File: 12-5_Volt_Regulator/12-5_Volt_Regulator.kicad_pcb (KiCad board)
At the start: 2 copper layers, 44.4 x 31.8 mm, 23 parts, among them J1 Conn_01x02, J2 Conn_01x02, U1 LM22676MR-5

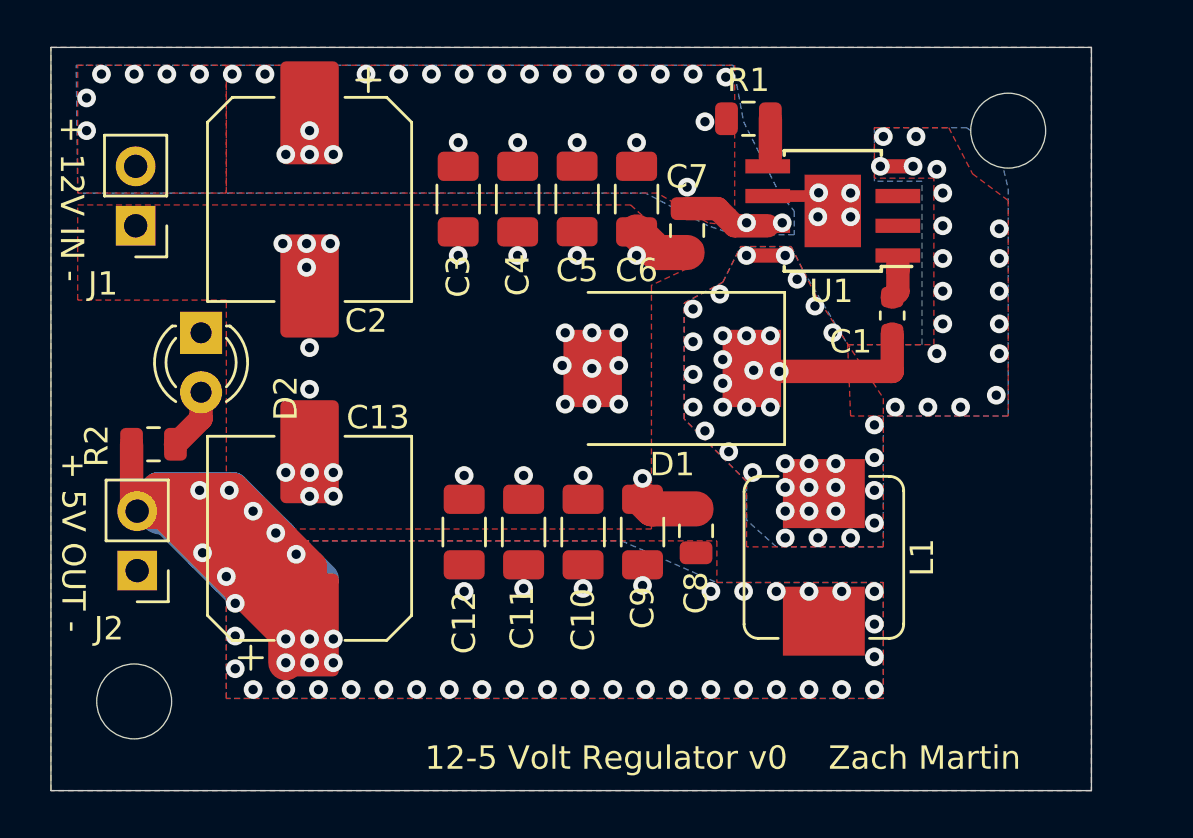
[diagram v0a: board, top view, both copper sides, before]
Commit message: Added wire pads, removed vias & fills as I switched grid spacing
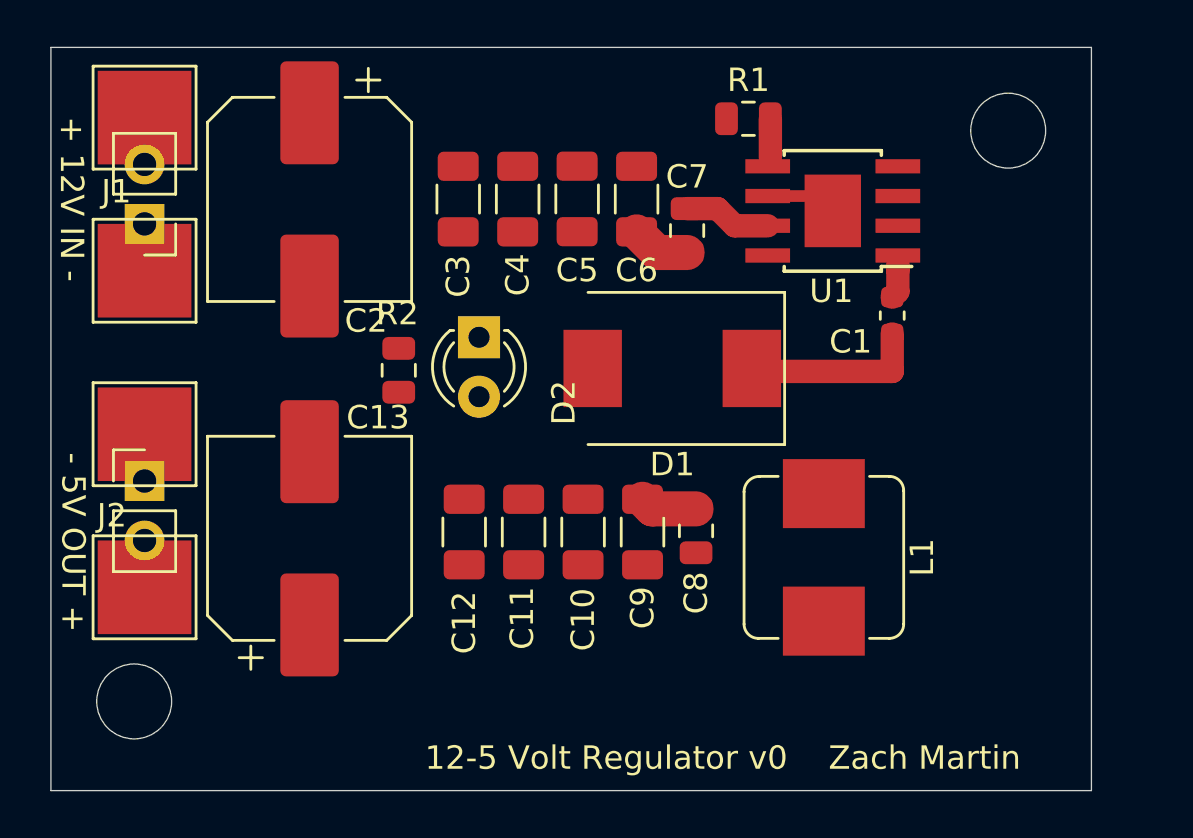
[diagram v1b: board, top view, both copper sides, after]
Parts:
- added REF**: TestPoint_Pad_4.0x4.0mm, TestPoint:TestPoint_Pad_4.0x4.0mm, F.Cu at (120.5, 112.5)
- added REF**: TestPoint_Pad_4.0x4.0mm, TestPoint:TestPoint_Pad_4.0x4.0mm, F.Cu at (120.5, 105.9)
- added REF**: TestPoint_Pad_4.0x4.0mm, TestPoint:TestPoint_Pad_4.0x4.0mm, F.Cu at (120.5, 98.9)
- added REF**: TestPoint_Pad_4.0x4.0mm, TestPoint:TestPoint_Pad_4.0x4.0mm, F.Cu at (120.5, 92.4)
- moved D2 11.9 mm to (134.7, 101.8)
- moved R2 10.9 mm to (131.3, 103.2), turned to 270 degrees
- moved J2 3.84 mm to (120.5, 107.9), turned to 0 degrees
- moved J1 0.39 mm to (120.5, 96.9)
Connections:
- D2 pad 1: GND -> Net-(D2-Pad1)
- D2 pad 2: Net-(D2-Pad2) -> /5v
- R2 pad 1: /5v -> Net-(D2-Pad1)
- R2 pad 2: Net-(D2-Pad2) -> GND
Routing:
- net /5v: track 60.1 -> 0.00 mm, vias 48 -> 0
- net Net-(D2-Pad2): track 2.81 -> 0.00 mm
- net GND: vias 32 -> 0
- net /V_SW: vias 59 -> 0
- net /12v: vias 32 -> 0
- removed copper zone on B.Cu, net /12v
- removed copper zone on F.Cu, net /12v
- removed copper zone on B.Cu, net /5v
- removed copper zone on F.Cu, net /5v
- removed copper zone on B.Cu, net /V_SW
- removed copper zone on F.Cu, net /V_SW
- removed copper zone on B.Cu, net GND
- removed copper zone on F.Cu, net GND
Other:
- board text added: "- 5V OUT +"
- board text removed: "+ 5V OUT -"

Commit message: Re-routed zone boundaries
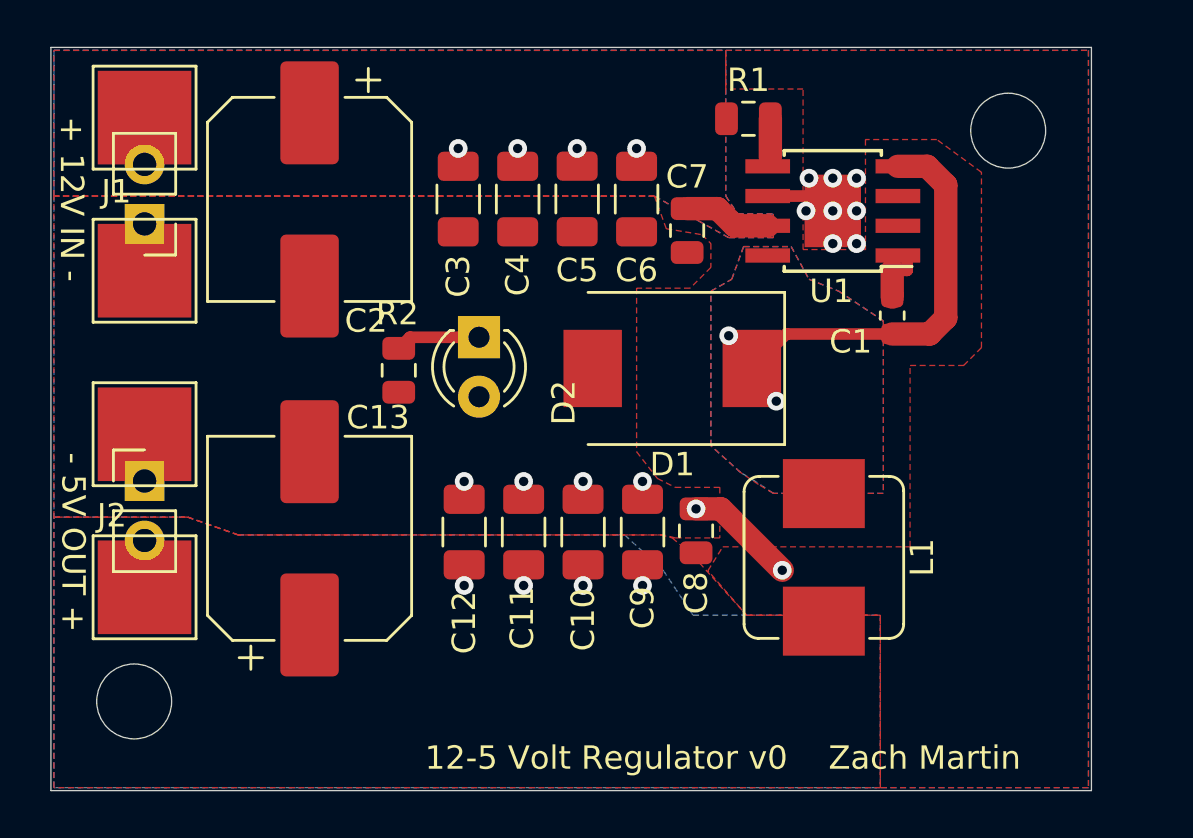
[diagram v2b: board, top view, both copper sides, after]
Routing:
- net /V_SW: track 8.01 -> 17.6 mm, vias 0 -> 2
- net Net-(D2-Pad1): track 0.00 -> 3.63 mm
- net Net-(C1-Pad2): track 2.12 -> 2.89 mm
- net GND: track 7.22 -> 7.00 mm, vias 0 -> 14
- net /5v: vias 0 -> 4
- net /12v: vias 0 -> 4
- added copper zone on B.Cu, net /12v
- added copper zone on F.Cu, net /12v
- added copper zone on B.Cu, net /5v
- added copper zone on F.Cu, net /5v
- added copper zone on B.Cu, net /V_SW
- added copper zone on F.Cu, net /V_SW
- added copper zone on B.Cu, net GND
- added copper zone on F.Cu, net GND

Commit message: Updated vias, traces, fills, JLCPCB part # location. Ready for ordering
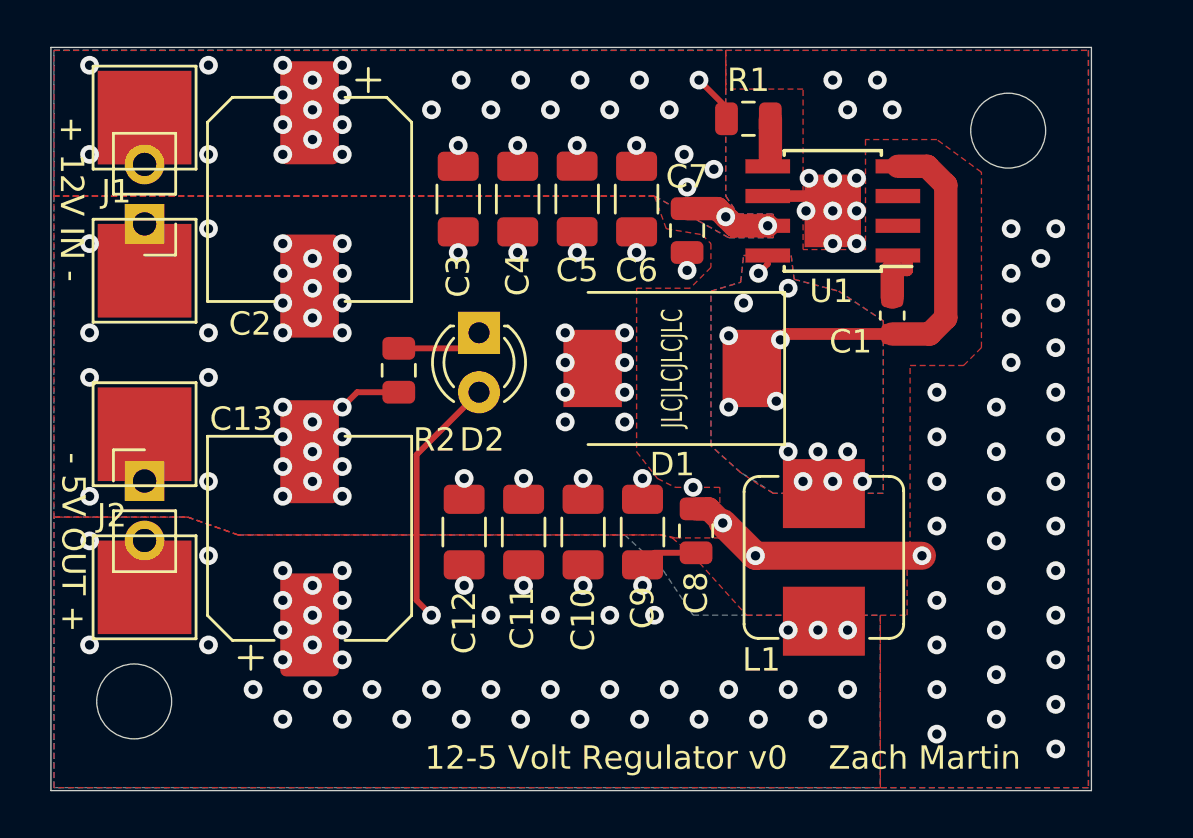
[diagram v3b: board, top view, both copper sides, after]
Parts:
- moved D2 0.19 mm to (134.7, 101.6)
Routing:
- net /5v: track 0.00 -> 13.4 mm, vias 4 -> 48
- net GND: track 7.00 -> 15.4 mm, vias 14 -> 96
- net /12v: track 3.75 -> 5.88 mm, vias 4 -> 34
- net /V_SW: track 17.6 -> 18.5 mm, vias 2 -> 13
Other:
- board text added: "JLCJLCJLCJLC"
